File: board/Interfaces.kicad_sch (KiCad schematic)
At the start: 6 parts, among them U2 ATA6561

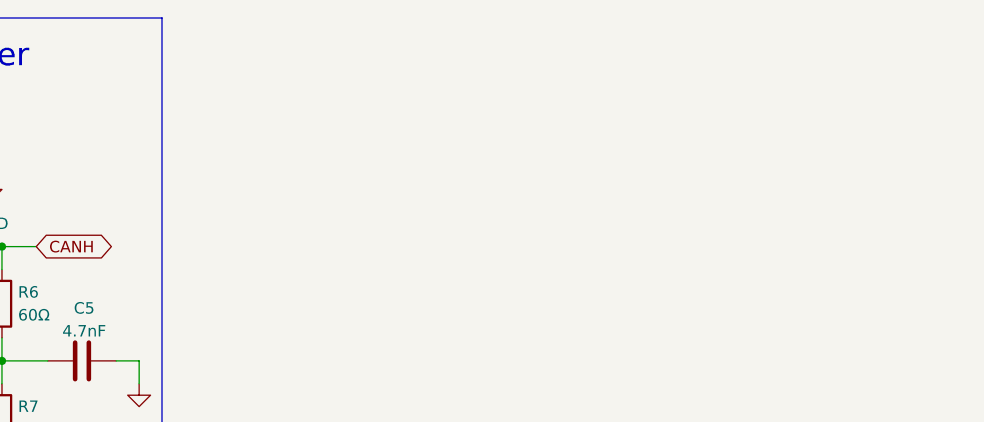
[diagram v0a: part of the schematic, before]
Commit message: Added CAN and Encoder connectors.
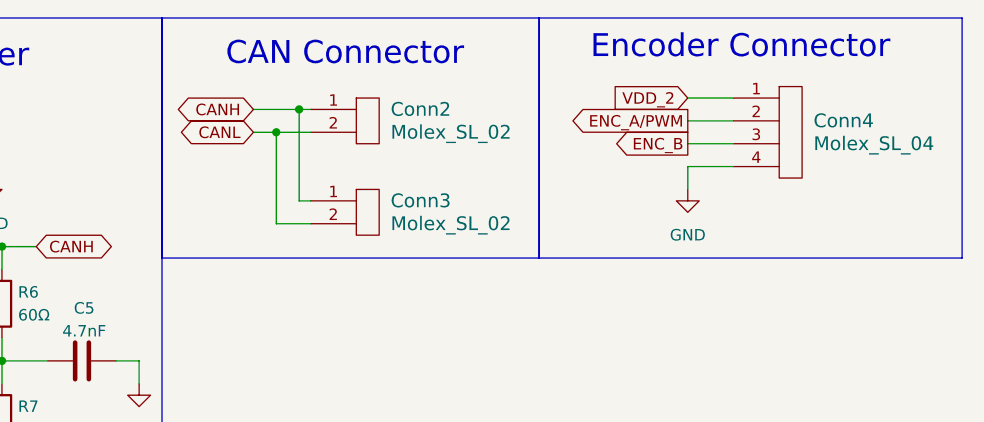
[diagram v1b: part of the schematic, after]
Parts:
- added Conn2, Conn3: Molex_SL_02, symbol MRDT_Connectors:Molex_SL_02
- added Conn4: Molex_SL_04, symbol MRDT_Connectors:Molex_SL_04
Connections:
- net CANH: now also Conn2.1, Conn3.1
- net CANL: now also Conn2.2, Conn3.2
- net GND: now also Conn4.4
- new net ENC_A/PWM: Conn4.2
- new net ENC_B: Conn4.3
- new net VDD_2: Conn4.1
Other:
- note added: "CAN Connector"
- note added: "Encoder Connector"

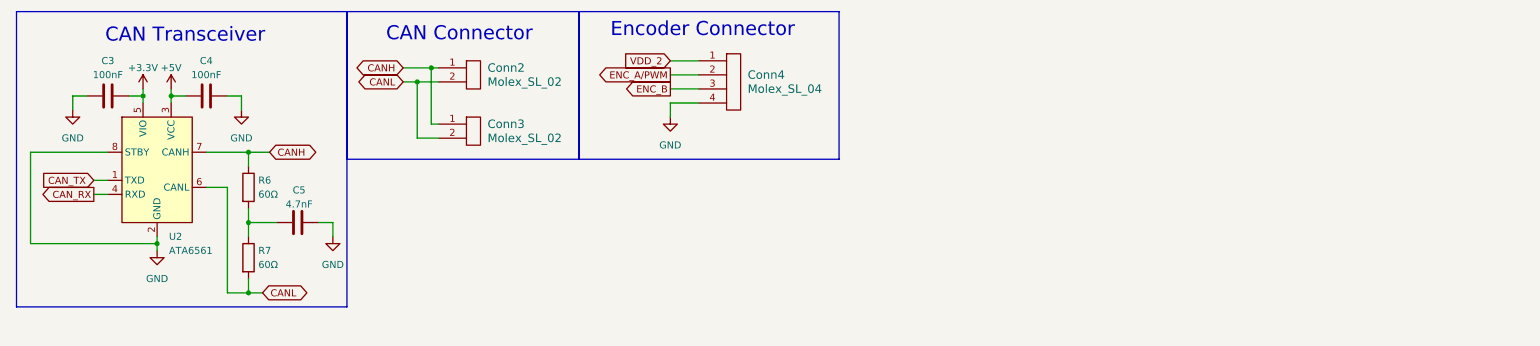
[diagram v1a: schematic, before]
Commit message: Implemented some fixes discussed during the board review.
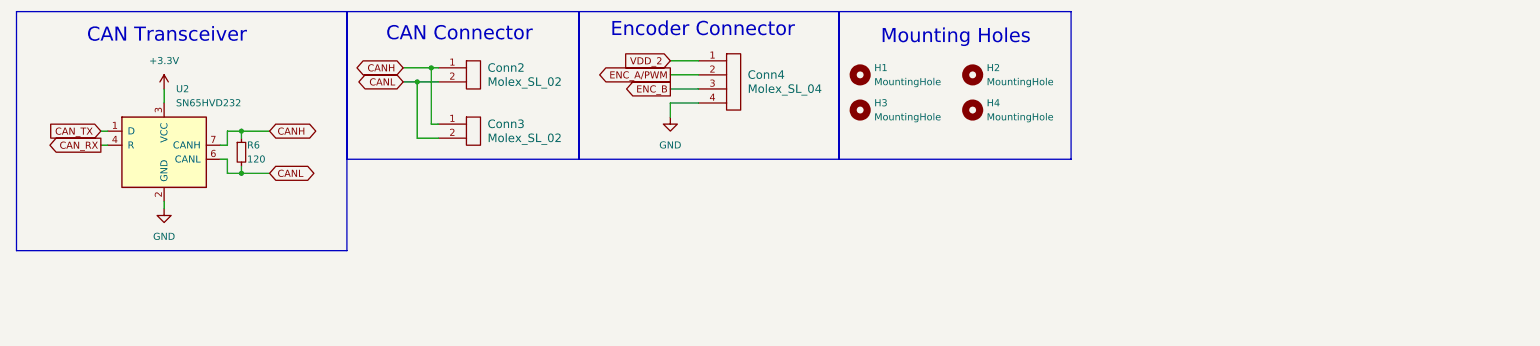
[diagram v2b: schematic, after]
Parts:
- removed C3, C4: 100nF, symbol Device:C
- removed C5: 4.7nF, symbol Device:C
- removed R6, R7: 60Ω, symbol Device:R
- removed U2: ATA6561, Package_SO:SOIC-8_3.9x4.9mm_P1.27mm, symbol MRDT_Devices:ATA6561
- added H1, H2, H3, H4: MountingHole, symbol Mechanical:MountingHole
- added R6: 120, Resistor_SMD:R_0603_1608Metric_Pad0.98x0.95mm_HandSolder, symbol Device:R_Small
- added U2: SN65HVD232, Package_SO:SOIC-8_3.9x4.9mm_P1.27mm, symbol Interface_CAN_LIN:SN65HVD232
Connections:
- net +3.3V: now also U2.3 (VCC)
- net CANH: now also R6.1, U2.7 (CANH)
- net CANL: now also R6.2, U2.6 (CANL)
- net CAN_RX: now also U2.4 (R)
- net CAN_TX: now also U2.1 (D)
- net GND: now also U2.2 (GND)
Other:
- note added: "Mounting Holes"

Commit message: Fixed many issues brought up in the schematic review.
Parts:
- added Conn1, Conn5, Conn6: AndersonPP, symbol MRDT_Connectors:AndersonPP
- added J5: Conn_01x04, Connector_PinSocket_2.54mm:PinSocket_1x04_P2.54mm_Vertical, symbol Connector_Generic:Conn_01x04
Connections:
- net VDD_2 is gone; now on net +3.3V: Conn4.1
- net GND: now also J5.4 (Pin_4)
- new net +3V3: J5.1 (Pin_1)
- new net PHASE_U: Conn1.1
- new net PHASE_V: Conn5.1
- new net PHASE_W: Conn6.1
- new net SWCLK: J5.2 (Pin_2)
- new net SWDIO: J5.3 (Pin_3)
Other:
- note added: "Motor Connectors"
- note added: "SWD Connector"
- moved on the sheet: Conn4

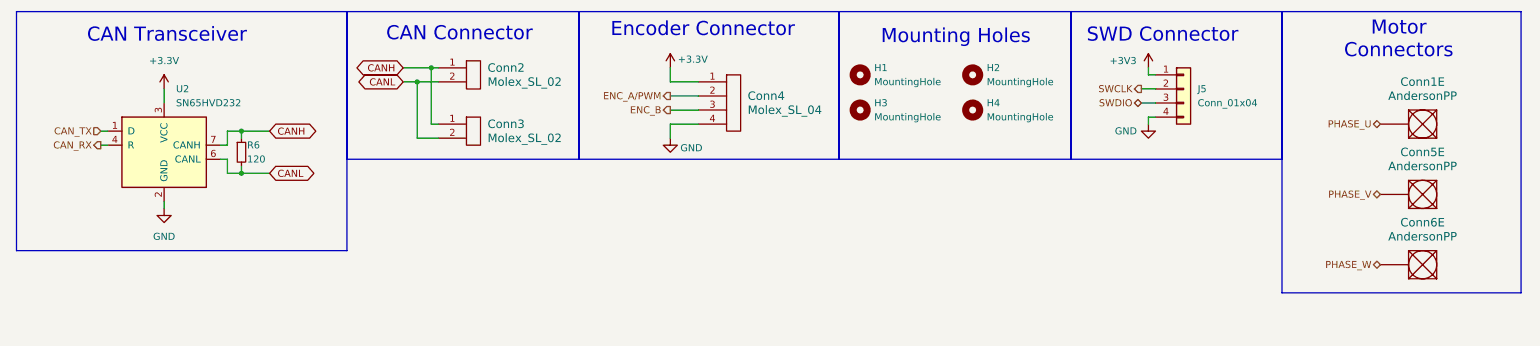
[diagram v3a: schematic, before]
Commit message: Fixed everything mentioned in schematic review, should be ready for second review/layout.
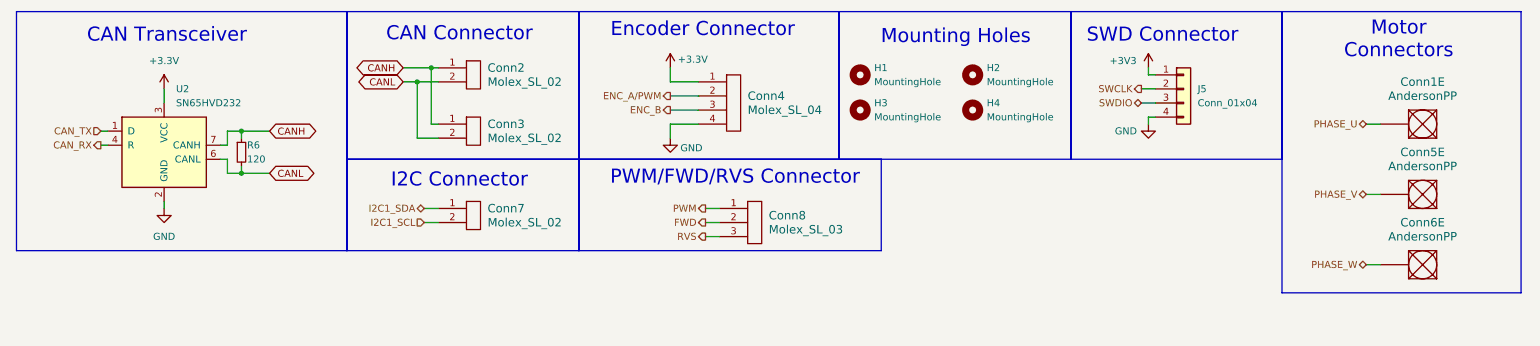
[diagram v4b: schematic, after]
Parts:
- added Conn7: Molex_SL_02, symbol MRDT_Connectors:Molex_SL_02
- added Conn8: Molex_SL_03, symbol MRDT_Connectors:Molex_SL_03
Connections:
- new net FWD: Conn8.2
- new net I2C1_SCL: Conn7.2
- new net I2C1_SDA: Conn7.1
- new net PWM: Conn8.1
- new net RVS: Conn8.3
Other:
- note added: "I2C Connector"
- note added: "PWM/FWD/RVS Connector"

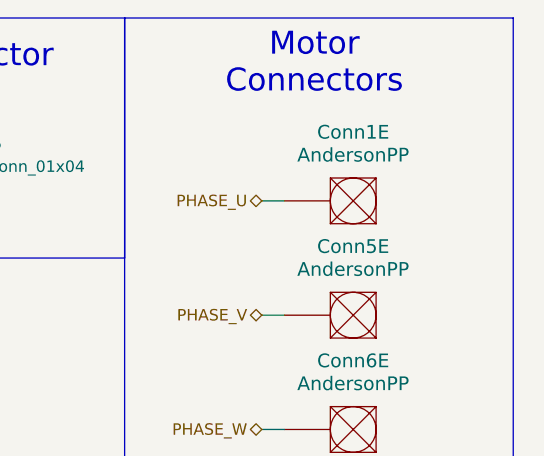
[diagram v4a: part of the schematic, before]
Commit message: Adjusted schematic footprints
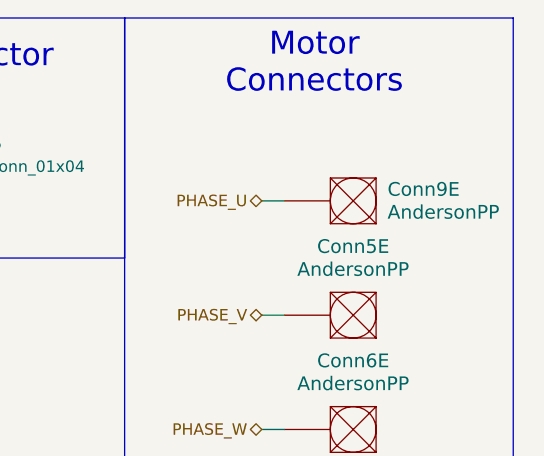
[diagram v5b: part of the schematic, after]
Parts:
- Conn2, Conn3, Conn7: footprint (none) -> MRDT_Connectors:MOLEX_SL_02_Horizontal
- Conn4: footprint (none) -> MRDT_Connectors:MOLEX_SL_04_Horizontal
- Conn5, Conn6: footprint (none) -> MRDT_Connectors:Square_Anderson_1_H
- Conn8: footprint (none) -> MRDT_Connectors:MOLEX_SL_03_Horizontal
- Conn9: renamed from Conn1; footprint (none) -> MRDT_Connectors:Square_Anderson_1_H
- H1, H2, H3, H4: footprint (none) -> MRDT_Drill_Holes:4_40_Hole
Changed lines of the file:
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@@
 			)
 		)
-		(property "Footprint" ""
+		(property "Footprint" "MRDT_Connectors:Square_Anderson_1_H"
 			(at 273.05 74.93 0)
 			(effects
@@
 			)
 		)
-		(property "Footprint" ""
+		(property "Footprint" "MRDT_Connectors:MOLEX_SL_02_Horizontal"
 			(at 93.98 54.61 0)
 			(effects
@@
 			)
 		)
-		(property "Footprint" ""
+		(property "Footprint" "MRDT_Connectors:Square_Anderson_1_H"
 			(at 273.05 62.23 0)
 			(effects
@@
 			)
 		)
-		(property "Footprint" ""
+		(property "Footprint" "MRDT_Connectors:MOLEX_SL_04_Horizontal"
 			(at 140.97 34.29 0)
 			(effects
@@
 			)
 		)
-		(property "Footprint" ""
+		(property "Footprint" "MRDT_Drill_Holes:4_40_Hole"
 			(at 165.1 30.48 0)
 			(effects
@@
 		(dnp no)
 		(fields_autoplaced yes)
-		(property "Reference" "Conn1"
-			(at 266.7 25.4 0)
-			(effects
-				(font
-					(size 1.524 1.524)
-				)
+		(property "Reference" "Conn9"
+			(at 270.51 31.7499 0)
+			(effects
+				(font
+					(size 1.524 1.524)
+				)
+				(justify right)
 			)
 		)
 		(property "Value" "AndersonPP"
-			(at 266.7 27.94 0)
-			(effects
-				(font
-					(size 1.524 1.524)
-				)
-			)
-		)
-		(property "Footprint" ""
+			(at 270.51 34.2899 0)
+			(effects
+				(font
+					(size 1.524 1.524)
+				)
+				(justify right)
+			)
+		)
+		(property "Footprint" "MRDT_Connectors:Square_Anderson_1_H"
 			(at 273.05 49.53 0)
 			(effects
@@
 			(project ""
 				(path "/1ef8bc88-f0df-4a97-862b-c4b9ec3b4ed0/d7362136-21d9-4887-9bf6-d218f0370e31"
-					(reference "Conn1")
+					(reference "Conn9")
 					(unit 5)
 				)
@@
 			)
 		)
-		(property "Footprint" ""
+		(property "Footprint" "MRDT_Drill_Holes:4_40_Hole"
 			(at 185.42 30.48 0)
 			(effects
@@
 			)
 		)
-		(property "Footprint" ""
+		(property "Footprint" "MRDT_Drill_Holes:4_40_Hole"
 			(at 185.42 24.13 0)
 			(effects
@@
 			)
 		)
-		(property "Footprint" ""
+		(property "Footprint" "MRDT_Connectors:MOLEX_SL_03_Horizontal"
 			(at 144.78 54.61 0)
 			(effects
@@
 			)
 		)
-		(property "Footprint" ""
+		(property "Footprint" "MRDT_Connectors:MOLEX_SL_02_Horizontal"
 			(at 93.98 29.21 0)
 			(effects
@@
 			)
 		)
-		(property "Footprint" ""
+		(property "Footprint" "MRDT_Connectors:MOLEX_SL_02_Horizontal"
 			(at 93.98 39.37 0)
 			(effects
@@
 			)
 		)
-		(property "Footprint" ""
+		(property "Footprint" "MRDT_Drill_Holes:4_40_Hole"
 			(at 165.1 24.13 0)
 			(effects

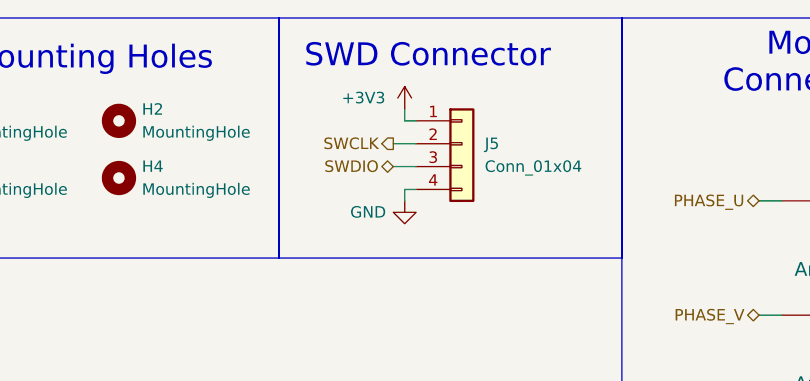
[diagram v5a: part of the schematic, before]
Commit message: Placed some basic planes in the layout and swapped mosfet symbols to match layout footprints.
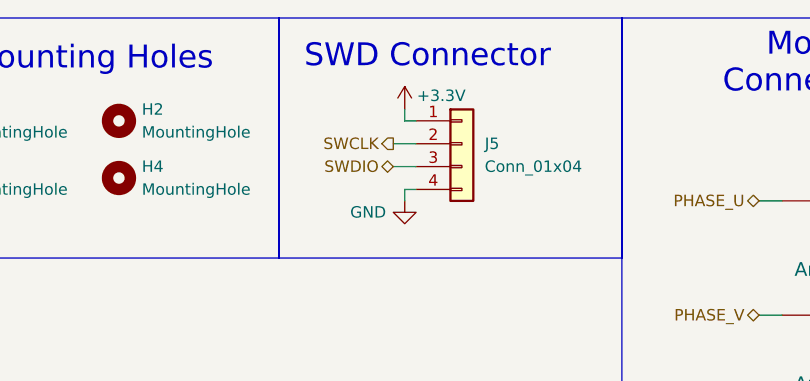
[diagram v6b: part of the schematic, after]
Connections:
- net +3V3 is gone; now on net +3.3V: J5.1 (Pin_1)
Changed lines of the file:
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@@
 	)
 	(symbol
-		(lib_id "power:+3V3")
+		(lib_id "power:+3.3V")
 		(at 217.17 22.86 0)
 		(unit 1)
@@
 			)
 		)
-		(property "Value" "+3V3"
-			(at 212.598 21.59 0)
+		(property "Value" "+3.3V"
+			(at 221.234 21.336 0)
 			(effects
 				(font
@@
 			)
 		)
-		(property "Description" "Power symbol creates a global label with name \"+3V3\""
+		(property "Description" "Power symbol creates a global label with name \"+3.3V\""
 			(at 217.17 22.86 0)
 			(effects

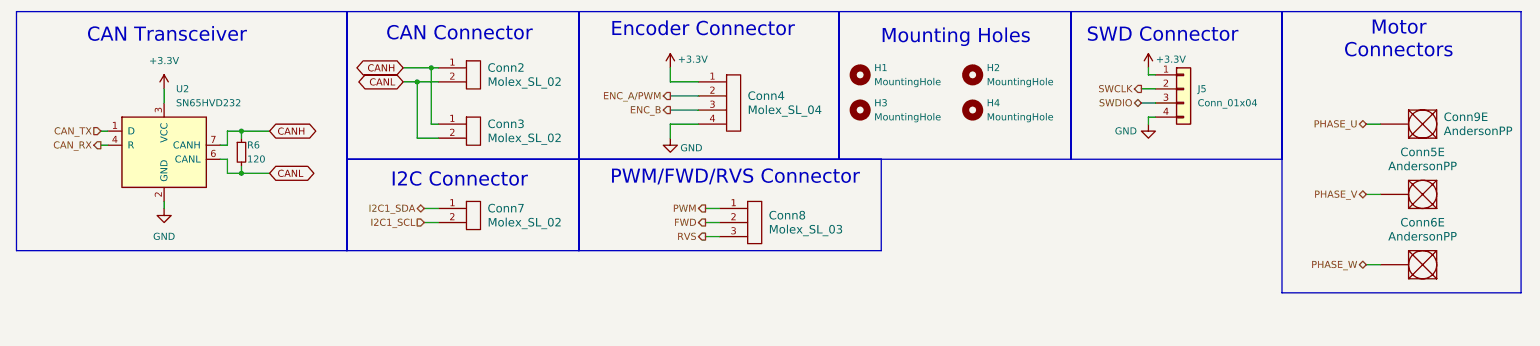
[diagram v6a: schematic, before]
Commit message: Significant progress on board layout. Added GPIO and UART pins, also rearranged encoder and I2C MCU pins.
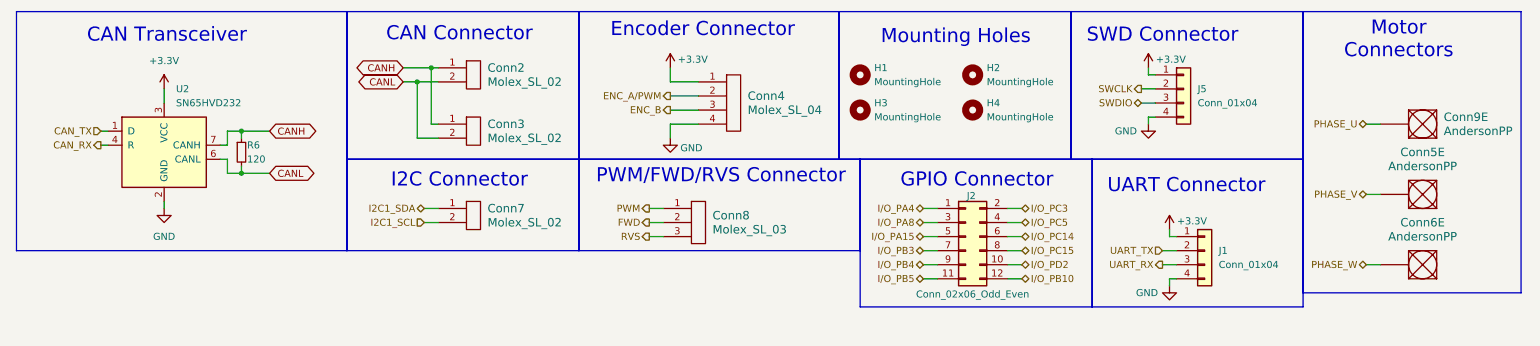
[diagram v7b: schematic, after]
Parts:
- added J1: Conn_01x04, Connector_PinSocket_2.54mm:PinSocket_1x04_P2.54mm_Vertical, symbol Connector_Generic:Conn_01x04
- added J2: Conn_02x06_Odd_Even, Connector_PinSocket_2.54mm:PinSocket_2x06_P2.54mm_Vertical, symbol Connector_Generic:Conn_02x06_Odd_Even
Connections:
- net +3.3V: now also J1.1 (Pin_1)
- net GND: now also J1.4 (Pin_4)
- new net I/O_PA15: J2.5 (Pin_5)
- new net I/O_PA4: J2.1 (Pin_1)
- new net I/O_PA8: J2.3 (Pin_3)
- new net I/O_PB10: J2.12 (Pin_12)
- new net I/O_PB3: J2.7 (Pin_7)
- new net I/O_PB4: J2.9 (Pin_9)
- new net I/O_PB5: J2.11 (Pin_11)
- new net I/O_PC14: J2.6 (Pin_6)
- new net I/O_PC15: J2.8 (Pin_8)
- new net I/O_PC3: J2.2 (Pin_2)
- new net I/O_PC5: J2.4 (Pin_4)
- new net I/O_PD2: J2.10 (Pin_10)
- new net UART_RX: J1.3 (Pin_3)
- new net UART_TX: J1.2 (Pin_2)
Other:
- note added: "GPIO Connector"
- note added: "UART Connector"
- moved on the sheet: Conn8

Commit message: Updated footprints to fix issues found in board review.
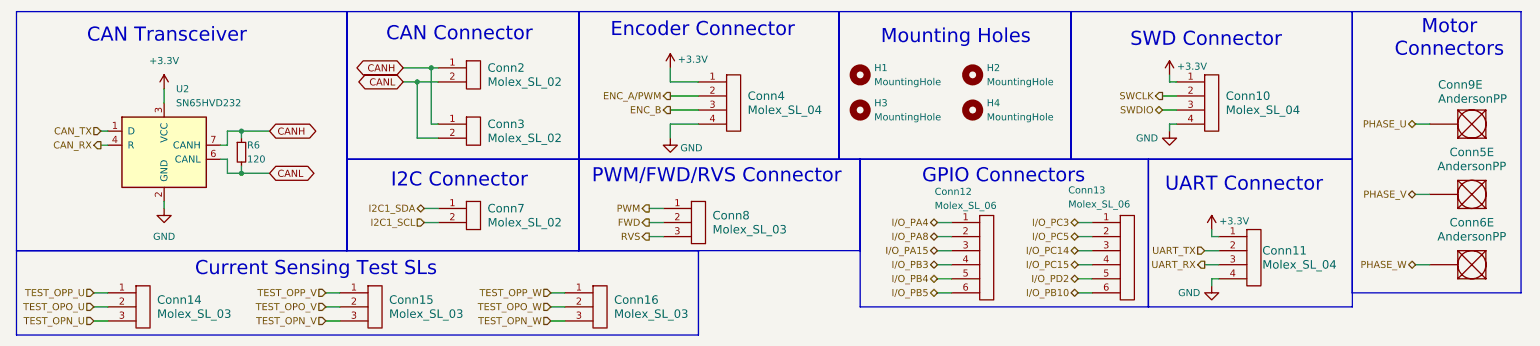
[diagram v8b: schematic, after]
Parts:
- removed J1, J5: Conn_01x04, Connector_PinSocket_2.54mm:PinSocket_1x04_P2.54mm_Vertical, symbol Connector_Generic:Conn_01x04
- removed J2: Conn_02x06_Odd_Even, Connector_PinSocket_2.54mm:PinSocket_2x06_P2.54mm_Vertical, symbol Connector_Generic:Conn_02x06_Odd_Even
- added Conn10, Conn11: Molex_SL_04, MRDT_Connectors:MOLEX_SL_04_Vertical, symbol MRDT_Connectors:Molex_SL_04
- added Conn12, Conn13: Molex_SL_06, MRDT_Connectors:MOLEX_SL_06_Vertical, symbol MRDT_Connectors:Molex_SL_06
- added Conn14, Conn15, Conn16: Molex_SL_03, MRDT_Connectors:MOLEX_SL_03_Vertical, symbol MRDT_Connectors:Molex_SL_03
- Conn2, Conn3, Conn7: footprint MRDT_Connectors:MOLEX_SL_02_Horizontal -> MRDT_Connectors:MOLEX_SL_02_Vertical
- Conn4: footprint MRDT_Connectors:MOLEX_SL_04_Horizontal -> MRDT_Connectors:MOLEX_SL_04_Vertical
- Conn8: footprint MRDT_Connectors:MOLEX_SL_03_Horizontal -> MRDT_Connectors:MOLEX_SL_03_Vertical
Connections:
- net +3.3V: now also Conn10.1, Conn11.1
- net GND: now also Conn10.4, Conn11.4
- net I/O_PA15: now also Conn12.3
- net I/O_PA4: now also Conn12.1
- net I/O_PA8: now also Conn12.2
- net I/O_PB10: now also Conn13.6
- net I/O_PB3: now also Conn12.4
- net I/O_PB4: now also Conn12.5
- net I/O_PB5: now also Conn12.6
- net I/O_PC14: now also Conn13.3
- net I/O_PC15: now also Conn13.4
- net I/O_PC3: now also Conn13.1
- net I/O_PC5: now also Conn13.2
- net I/O_PD2: now also Conn13.5
- net SWCLK: now also Conn10.2
- net SWDIO: now also Conn10.3
- net UART_RX: now also Conn11.3
- net UART_TX: now also Conn11.2
- new net TEST_OPN_U: Conn14.3
- new net TEST_OPN_V: Conn15.3
- new net TEST_OPN_W: Conn16.3
- new net TEST_OPO_U: Conn14.2
- new net TEST_OPO_V: Conn15.2
- new net TEST_OPO_W: Conn16.2
- new net TEST_OPP_U: Conn14.1
- new net TEST_OPP_V: Conn15.1
- new net TEST_OPP_W: Conn16.1
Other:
- note added: "Current Sensing Test SLs"
- note added: "GPIO Connectors"
- note removed: "GPIO Connector"
- moved on the sheet: Conn5E, Conn6E, Conn9E
